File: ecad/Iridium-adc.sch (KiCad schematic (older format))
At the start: 0 parts

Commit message: Mostly complete schematic, about to tape out the PCB.
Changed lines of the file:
@@
 LIBS:contrib
 LIBS:valves
+LIBS:custom-parts
 LIBS:dk_Addressable-Specialty
 LIBS:dk_Alarms-Buzzers-and-Sirens
@@
 LIBS:dk_Clock-Timing-Programmable-Timers-and-Oscillators
 LIBS:dk_Clock-Timing-Real-Time-Clocks
-LIBS:dk_Coaxial-Connectors-(RF)
+LIBS:dk_Coaxial-Connectors-RF
 LIBS:dk_Current-Transducers
 LIBS:dk_Data-Acquisition-ADCs-DACs-Special-Purpose
-LIBS:dk_Data-Acquisition-Analog-to-Digital-Converters-(ADC)
+LIBS:dk_Data-Acquisition-Analog-to-Digital-Converters-ADC
 LIBS:dk_Data-Acquisition-Digital-Potentiometers
-LIBS:dk_Data-Acquisition-Digital-to-Analog-Converters-(DAC)
+LIBS:dk_Data-Acquisition-Digital-to-Analog-Converters-DAC
 LIBS:dk_Data-Acquisition-Touch-Screen-Controllers
 LIBS:dk_DC-DC-Converters
@@
 LIBS:dk_Image-Sensors-Camera
 LIBS:dk_Infrared-UV-Visible-Emitters
-LIBS:dk_Inrush-Current-Limiters-(ICL)
+LIBS:dk_Inrush-Current-Limiters-ICL
 LIBS:dk_Interface-Analog-Switches-Multiplexers-Demultiplexers
 LIBS:dk_Interface-Analog-Switches-Special-Purpose
@@
 LIBS:dk_Logic-Signal-Switches-Multiplexers-Decoders
 LIBS:dk_Logic-Translators-Level-Shifters
-LIBS:dk_Magnetic-Sensors-Compass-Magnetic-Field-(Modules)
-LIBS:dk_Magnetic-Sensors-Linear-Compass-(ICs)
-LIBS:dk_Magnetic-Sensors-Switches-(Solid-State)
+LIBS:dk_Magnetic-Sensors-Compass-Magnetic-Field-Modules
+LIBS:dk_Magnetic-Sensors-Linear-Compass-ICs
+LIBS:dk_Magnetic-Sensors-Switches-Solid-State
 LIBS:dk_Memory
 LIBS:dk_Memory-Connectors-PC-Card-Sockets
@@
 LIBS:dk_Modular-Connectors-Jacks-With-Magnetics
 LIBS:dk_Motion-Sensors-Accelerometers
-LIBS:dk_Motion-Sensors-IMUs-(Inertial-Measurement-Units)
+LIBS:dk_Motion-Sensors-IMUs-Inertial-Measurement-Units
 LIBS:dk_Motion-Sensors-Tilt-Switches
 LIBS:dk_Navigation-Switches-Joystick
@@
 LIBS:dk_Tactile-Switches
 LIBS:dk_Temperature-Sensors-Analog-and-Digital-Output
-LIBS:dk_Thermal-Cutoffs-(Thermal-Fuses)
+LIBS:dk_Thermal-Cutoffs-Thermal-Fuses
 LIBS:dk_Thyristors-DIACs-SIDACs
 LIBS:dk_Thyristors-SCRs
 LIBS:dk_Thyristors-TRIACs
 LIBS:dk_Toggle-Switches
-LIBS:dk_Transistors-Bipolar-(BJT)-Arrays
-LIBS:dk_Transistors-Bipolar-(BJT)-RF
-LIBS:dk_Transistors-Bipolar-(BJT)-Single
-LIBS:dk_Transistors-Bipolar-(BJT)-Single-Pre-Biased
+LIBS:dk_Transistors-Bipolar-BJT-Arrays
+LIBS:dk_Transistors-Bipolar-BJT-RF
+LIBS:dk_Transistors-Bipolar-BJT-Single
+LIBS:dk_Transistors-Bipolar-BJT-Single-Pre-Biased
 LIBS:dk_Transistors-FETs-MOSFETs-Arrays
 LIBS:dk_Transistors-FETs-MOSFETs-RF
@@
 LIBS:dk_TVS-Mixed-Technology
 LIBS:dk_USB-DVI-HDMI-Connectors
-LIBS:custom-parts
 LIBS:Iridium-adc-cache
 EELAYER 25 0
@@
 $EndDescr
 $Sheet
+S 2100 3100 1600 1000
+U 5A77D384
+F0 "Input" 60
+F1 "input.sch" 60
+F2 "PreOutP" O R 3700 3950 60
+F3 "PreOutN" O R 3700 4050 60
+F4 "+12" I L 2100 3250 60
+F5 "BIAS" I L 2100 3350 60
+$EndSheet
+$Sheet
+S 4300 3100 1600 1000
+U 5A77D399
+F0 "ADC" 60
+F1 "adc.sch" 60
+F2 "Vdd4" I L 4300 3650 60
+F3 "Vdd1" I L 4300 3350 60
+F4 "Vdd2" I L 4300 3450 60
+F5 "Vdd3" I L 4300 3550 60
+F6 "VDrive" I L 4300 3250 60
+F7 "DVdd" I L 4300 3150 60
+F8 "4.096" I L 4300 3750 60
+F9 "~DRDY" O R 5900 3400 60
+F10 "~RESET" O R 5900 3500 60
+F11 "~SYNC" O R 5900 3600 60
+F12 "~RD" O R 5900 3700 60
+F13 "~CS" O R 5900 3800 60
+F14 "InputP" I L 4300 3950 60
+F15 "InputN" I L 4300 4050 60
+F16 "DB[15..0]" O R 5900 3250 60
+$EndSheet
+Wire Wire Line
+	3700 3950 4300 3950
+Wire Wire Line
+	4300 4050 3700 4050
+Wire Wire Line
+	2150 2050 2000 2050
+Wire Wire Line
+	2000 2050 2000 3250
+Wire Wire Line
+	2000 3250 2100 3250
+Wire Wire Line
+	2100 3350 1950 3350
+Wire Wire Line
+	1950 3350 1950 1950
+Wire Wire Line
+	1950 1950 2150 1950
+Wire Wire Line
+	3700 2050 3950 2050
+Wire Wire Line
+	3950 2050 3950 3750
+Wire Wire Line
+	3950 3750 4300 3750
+Wire Wire Line
+	3700 1750 4200 1750
+Wire Wire Line
+	4200 1750 4200 3350
+Wire Wire Line
+	4200 3150 4300 3150
+Wire Wire Line
+	4200 3250 4300 3250
+Connection ~ 4200 3150
+Wire Wire Line
+	4200 3350 4300 3350
+Connection ~ 4200 3250
+Wire Wire Line
+	3700 1850 4100 1850
+Wire Wire Line
+	4100 1850 4100 3650
+Wire Wire Line
+	4100 3450 4300 3450
+Wire Wire Line
+	4100 3550 4300 3550
+Connection ~ 4100 3450
+Wire Wire Line
+	4100 3650 4300 3650
+Connection ~ 4100 3550
+$Sheet
+S 6400 3100 1550 1000
+U 5A77D3A6
+F0 "Microcontroller" 60
+F1 "microcontroller.sch" 60
+F2 "DB[15..0]" I L 6400 3250 60
+F3 "~DRDY" I L 6400 3400 60
+F4 "~RESET" O L 6400 3500 60
+F5 "~CS" O L 6400 3800 60
+F6 "~RD" O L 6400 3700 60
+F7 "~SYNC" O L 6400 3600 60
+$EndSheet
+Wire Wire Line
+	5900 3400 6400 3400
+Wire Wire Line
+	5900 3500 6400 3500
+Wire Wire Line
+	5900 3600 6400 3600
+Wire Wire Line
+	5900 3700 6400 3700
+Wire Wire Line
+	5900 3800 6400 3800
+$Sheet
 S 2150 1150 1550 1050
 U 5A77D36E
 F0 "Power Supply" 60
 F1 "power-supply.sch" 60
-$EndSheet
-$Sheet
-S 2100 3100 1600 1000
-U 5A77D384
-F0 "Input" 60
-F1 "input.sch" 60
-$EndSheet
-$Sheet
-S 4300 3100 1600 1000
-U 5A77D399
-F0 "ADC" 60
-F1 "adc.sch" 60
-$EndSheet
-$Sheet
-S 6400 3100 1550 1000
-U 5A77D3A6
-F0 "Microcontroller" 60
-F1 "microcontroller.sch" 60
-$EndSheet
+F2 "+12" O L 2150 2050 60
+F3 "+5" O R 3700 1850 60
+F4 "4.096" O R 3700 2050 60
+F5 "BIAS" O L 2150 1950 60
+F6 "2.5V" O R 3700 1750 60
+$EndSheet
+Wire Bus Line
+	5900 3250 6400 3250
 $EndSCHEMATC

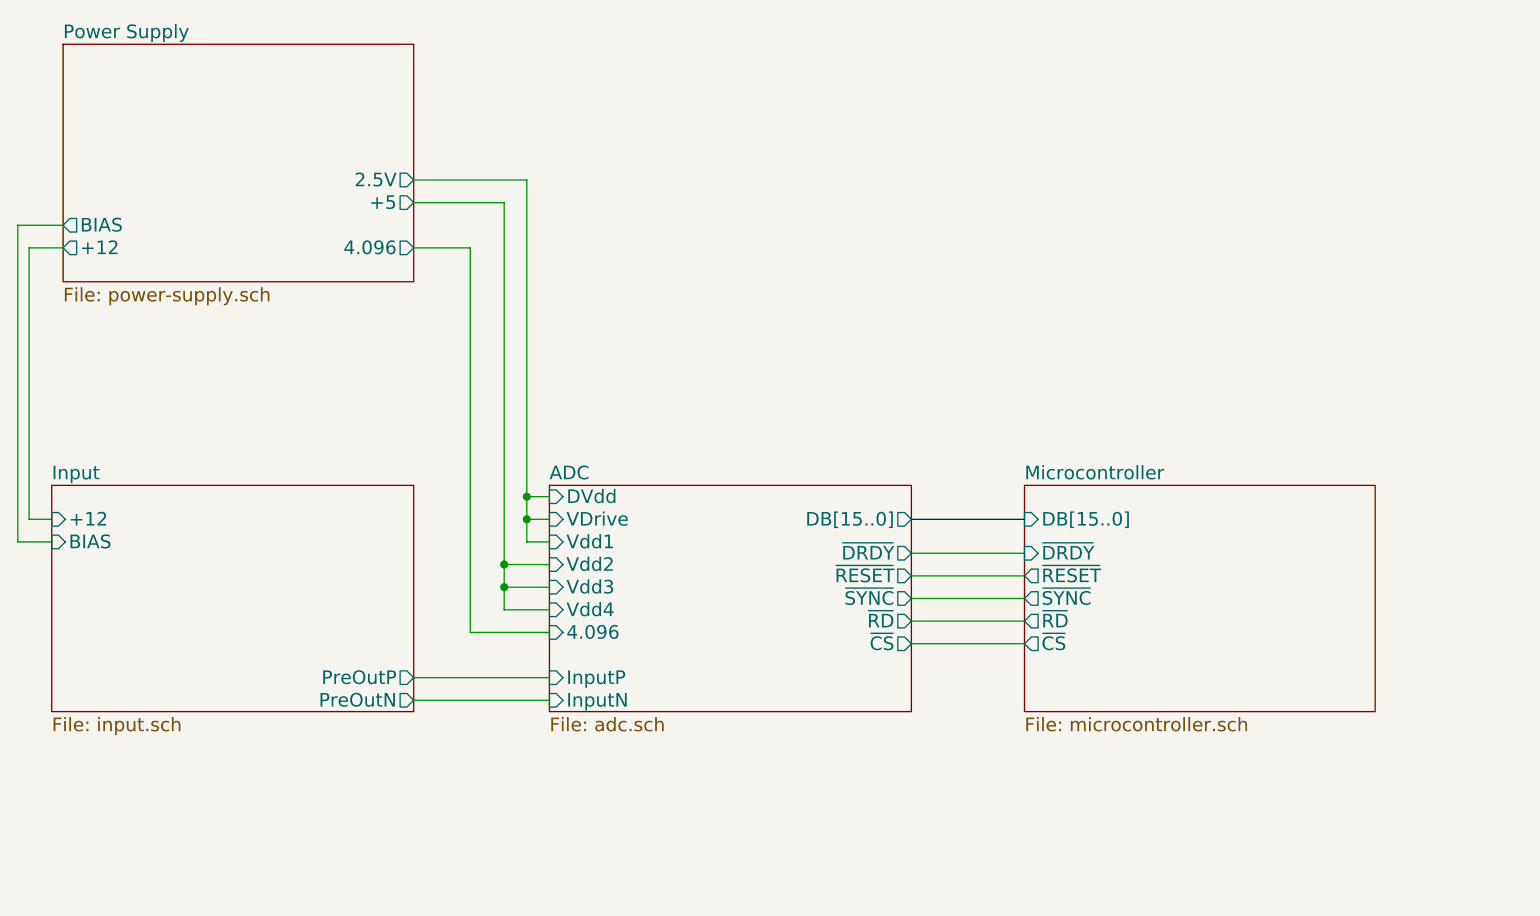
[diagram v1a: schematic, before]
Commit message: Slight changes to simulation and ecad with new changes before rollback to old changes.
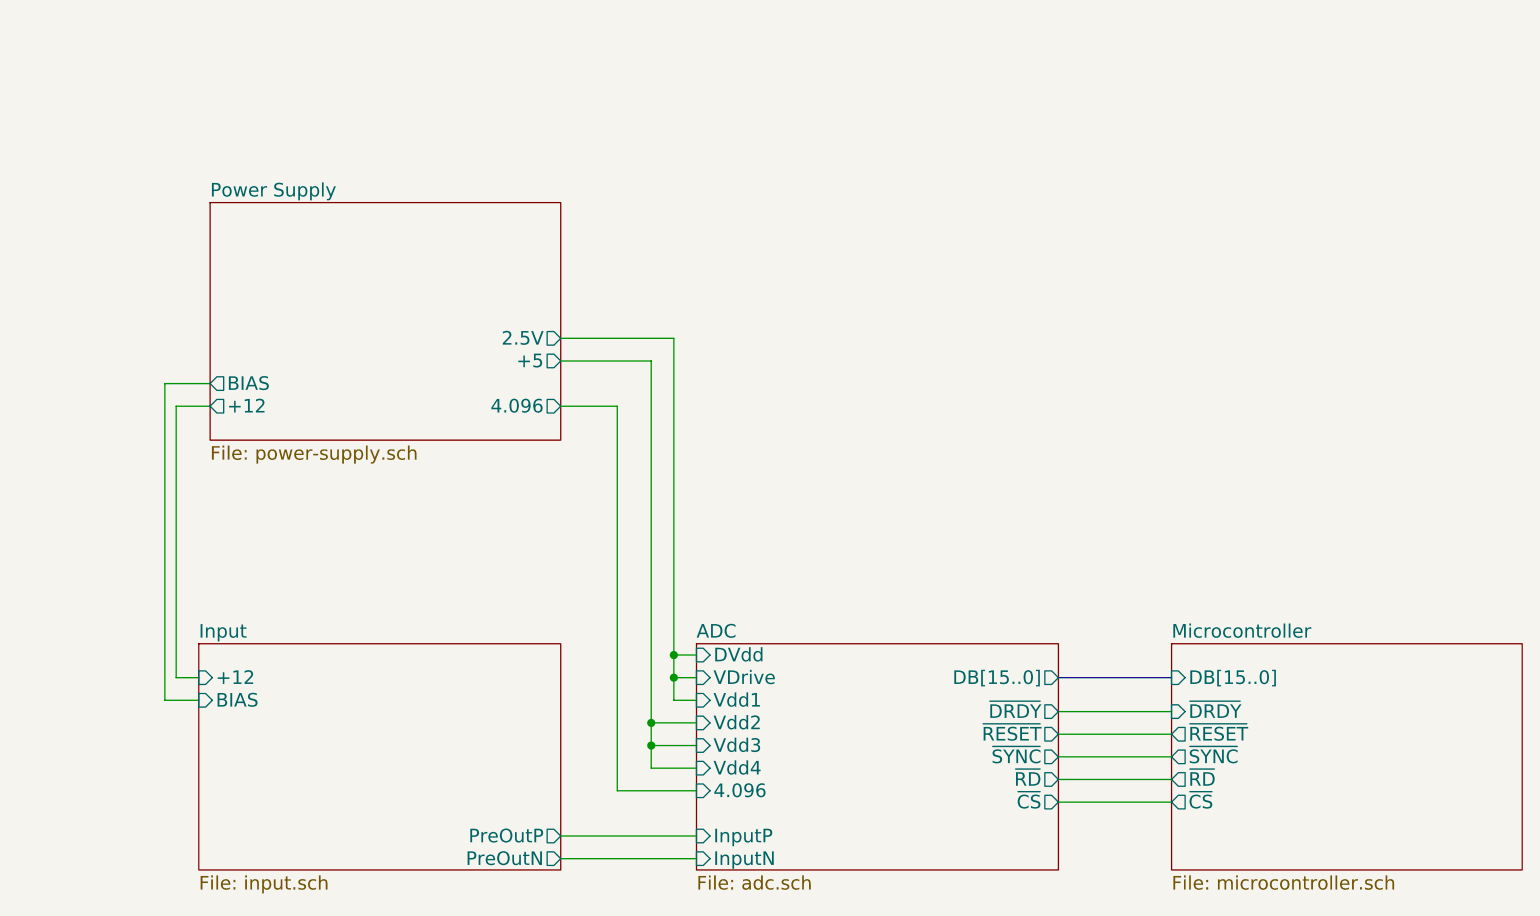
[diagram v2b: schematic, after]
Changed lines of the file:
@@
 EELAYER 25 0
 EELAYER END
-$Descr A4 11693 8268
+$Descr USLetter 11000 8500
 encoding utf-8
 Sheet 1 5
-Title ""
+Title "Iridium ADC"
 Date ""
 Rev ""
-Comp ""
+Comp "Billtech"
 Comment1 ""
 Comment2 ""
@@
 $EndDescr
 $Sheet
-S 2100 3100 1600 1000
+S 2750 3800 1600 1000
 U 5A77D384
 F0 "Input" 60
 F1 "input.sch" 60
-F2 "PreOutP" O R 3700 3950 60
-F3 "PreOutN" O R 3700 4050 60
-F4 "+12" I L 2100 3250 60
-F5 "BIAS" I L 2100 3350 60
+F2 "PreOutP" O R 4350 4650 60
+F3 "PreOutN" O R 4350 4750 60
+F4 "+12" I L 2750 3950 60
+F5 "BIAS" I L 2750 4050 60
 $EndSheet
 $Sheet
-S 4300 3100 1600 1000
+S 4950 3800 1600 1000
 U 5A77D399
 F0 "ADC" 60
 F1 "adc.sch" 60
-F2 "Vdd4" I L 4300 3650 60
-F3 "Vdd1" I L 4300 3350 60
-F4 "Vdd2" I L 4300 3450 60
-F5 "Vdd3" I L 4300 3550 60
-F6 "VDrive" I L 4300 3250 60
-F7 "DVdd" I L 4300 3150 60
-F8 "4.096" I L 4300 3750 60
-F9 "~DRDY" O R 5900 3400 60
-F10 "~RESET" O R 5900 3500 60
-F11 "~SYNC" O R 5900 3600 60
-F12 "~RD" O R 5900 3700 60
-F13 "~CS" O R 5900 3800 60
-F14 "InputP" I L 4300 3950 60
-F15 "InputN" I L 4300 4050 60
-F16 "DB[15..0]" O R 5900 3250 60
+F2 "Vdd4" I L 4950 4350 60
+F3 "Vdd1" I L 4950 4050 60
+F4 "Vdd2" I L 4950 4150 60
+F5 "Vdd3" I L 4950 4250 60
+F6 "VDrive" I L 4950 3950 60
+F7 "DVdd" I L 4950 3850 60
+F8 "4.096" I L 4950 4450 60
+F9 "~DRDY" O R 6550 4100 60
+F10 "~RESET" O R 6550 4200 60
+F11 "~SYNC" O R 6550 4300 60
+F12 "~RD" O R 6550 4400 60
+F13 "~CS" O R 6550 4500 60
+F14 "InputP" I L 4950 4650 60
+F15 "InputN" I L 4950 4750 60
+F16 "DB[15..0]" O R 6550 3950 60
 $EndSheet
 Wire Wire Line
-	3700 3950 4300 3950
+	4350 4650 4950 4650
 Wire Wire Line
-	4300 4050 3700 4050
+	4950 4750 4350 4750
 Wire Wire Line
-	2150 2050 2000 2050
+	2800 2750 2650 2750
 Wire Wire Line
-	2000 2050 2000 3250
+	2650 2750 2650 3950
 Wire Wire Line
-	2000 3250 2100 3250
+	2650 3950 2750 3950
 Wire Wire Line
-	2100 3350 1950 3350
+	2750 4050 2600 4050
 Wire Wire Line
-	1950 3350 1950 1950
+	2600 4050 2600 2650
 Wire Wire Line
-	1950 1950 2150 1950
+	2600 2650 2800 2650
 Wire Wire Line
-	3700 2050 3950 2050
+	4350 2750 4600 2750
 Wire Wire Line
-	3950 2050 3950 3750
+	4600 2750 4600 4450
 Wire Wire Line
-	3950 3750 4300 3750
+	4600 4450 4950 4450
 Wire Wire Line
-	3700 1750 4200 1750
+	4350 2450 4850 2450
 Wire Wire Line
-	4200 1750 4200 3350
+	4850 2450 4850 4050
 Wire Wire Line
-	4200 3150 4300 3150
+	4850 3850 4950 3850
 Wire Wire Line
-	4200 3250 4300 3250
-Connection ~ 4200 3150
+	4850 3950 4950 3950
+Connection ~ 4850 3850
 Wire Wire Line
-	4200 3350 4300 3350
-Connection ~ 4200 3250
+	4850 4050 4950 4050
+Connection ~ 4850 3950
 Wire Wire Line
-	3700 1850 4100 1850
+	4350 2550 4750 2550
 Wire Wire Line
-	4100 1850 4100 3650
+	4750 2550 4750 4350
 Wire Wire Line
-	4100 3450 4300 3450
+	4750 4150 4950 4150
 Wire Wire Line
-	4100 3550 4300 3550
-Connection ~ 4100 3450
+	4750 4250 4950 4250
+Connection ~ 4750 4150
 Wire Wire Line
-	4100 3650 4300 3650
-Connection ~ 4100 3550
+	4750 4350 4950 4350
+Connection ~ 4750 4250
 $Sheet
-S 6400 3100 1550 1000
+S 7050 3800 1550 1000
 U 5A77D3A6
 F0 "Microcontroller" 60
 F1 "microcontroller.sch" 60
-F2 "DB[15..0]" I L 6400 3250 60
-F3 "~DRDY" I L 6400 3400 60
-F4 "~RESET" O L 6400 3500 60
-F5 "~CS" O L 6400 3800 60
-F6 "~RD" O L 6400 3700 60
-F7 "~SYNC" O L 6400 3600 60
+F2 "DB[15..0]" I L 7050 3950 60
+F3 "~DRDY" I L 7050 4100 60
+F4 "~RESET" O L 7050 4200 60
+F5 "~CS" O L 7050 4500 60
+F6 "~RD" O L 7050 4400 60
+F7 "~SYNC" O L 7050 4300 60
 $EndSheet
 Wire Wire Line
-	5900 3400 6400 3400
+	6550 4100 7050 4100
 Wire Wire Line
-	5900 3500 6400 3500
+	6550 4200 7050 4200
 Wire Wire Line
-	5900 3600 6400 3600
+	6550 4300 7050 4300
 Wire Wire Line
-	5900 3700 6400 3700
+	6550 4400 7050 4400
 Wire Wire Line
-	5900 3800 6400 3800
+	6550 4500 7050 4500
 $Sheet
-S 2150 1150 1550 1050
+S 2800 1850 1550 1050
 U 5A77D36E
 F0 "Power Supply" 60
 F1 "power-supply.sch" 60
-F2 "+12" O L 2150 2050 60
-F3 "+5" O R 3700 1850 60
-F4 "4.096" O R 3700 2050 60
-F5 "BIAS" O L 2150 1950 60
-F6 "2.5V" O R 3700 1750 60
+F2 "+12" O L 2800 2750 60
+F3 "+5" O R 4350 2550 60
+F4 "4.096" O R 4350 2750 60
+F5 "BIAS" O L 2800 2650 60
+F6 "2.5V" O R 4350 2450 60
 $EndSheet
 Wire Bus Line
-	5900 3250 6400 3250
+	6550 3950 7050 3950
 $EndSCHEMATC
